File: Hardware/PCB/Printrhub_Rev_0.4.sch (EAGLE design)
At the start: 72 parts, among them J1 DM3D-SF, SW1 SPST_TACT-KMR2, SW2 SPST_TACT-KMR2, U1 MK20DX256VLH7, U2 AP1117E, U3 MAX308-SOT23, Y2 16Mhz/8pF

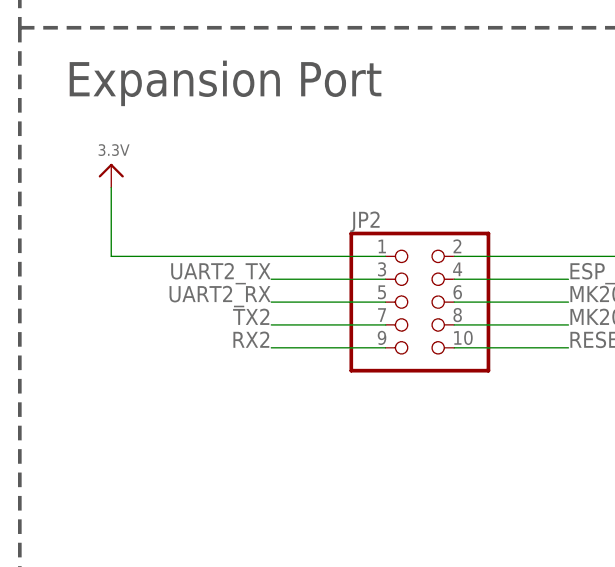
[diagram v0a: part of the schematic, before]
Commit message: Readded SCL1 and SDA1 (so this version is committed, too).
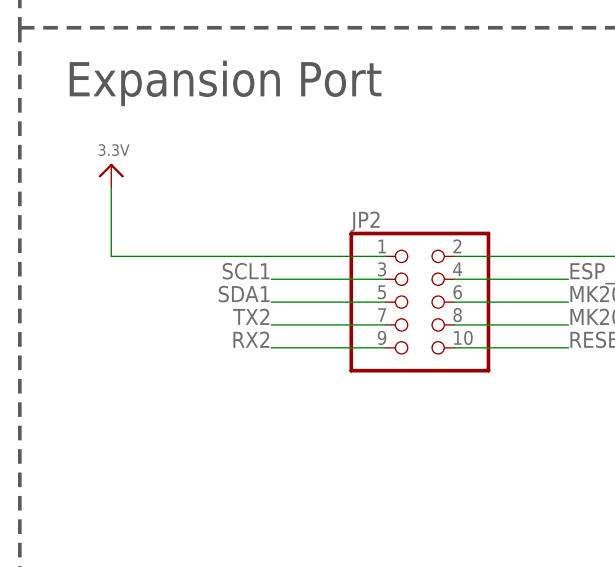
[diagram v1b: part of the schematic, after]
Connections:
- net SCL1: now also JP2.3
- net SDA1: now also JP2.5
- net UART2_RX: no longer JP2.5
- net UART2_TX: no longer JP2.3
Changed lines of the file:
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@@
 <label x="162.56" y="30.48" size="1.778" layer="95" rot="MR0"/>
-</segment>
-<segment>
-<pinref part="JP2" gate="A" pin="5"/>
-<wire x1="-71.12" y1="-104.14" x2="-83.82" y2="-104.14" width="0.1524" layer="91"/>
-<label x="-83.82" y="-104.14" size="1.778" layer="95" rot="MR0"/>
 </segment>
 </net>
@@
 <wire x1="177.8" y1="38.1" x2="162.56" y2="38.1" width="0.1524" layer="91"/>
 <label x="162.56" y="38.1" size="1.778" layer="95" rot="MR0"/>
-</segment>
-<segment>
-<pinref part="JP2" gate="A" pin="3"/>
-<wire x1="-71.12" y1="-101.6" x2="-83.82" y2="-101.6" width="0.1524" layer="91"/>
-<label x="-83.82" y="-101.6" size="1.778" layer="95" rot="MR0"/>
 </segment>
 </net>
@@
 <label x="187.96" y="-149.86" size="1.778" layer="95"/>
 </segment>
+<segment>
+<pinref part="JP2" gate="A" pin="3"/>
+<wire x1="-71.12" y1="-101.6" x2="-83.82" y2="-101.6" width="0.1524" layer="91"/>
+<label x="-83.82" y="-101.6" size="1.778" layer="95" rot="MR0"/>
+</segment>
 </net>
 <net name="SDA1" class="0">
@@
 <label x="187.96" y="-147.32" size="1.778" layer="95"/>
 </segment>
-</net>
+<segment>
+<pinref part="JP2" gate="A" pin="5"/>
+<wire x1="-71.12" y1="-104.14" x2="-83.82" y2="-104.14" width="0.1524" layer="91"/>
+<label x="-83.82" y="-104.14" size="1.778" layer="95" rot="MR0"/>
+</segment>
+</net>

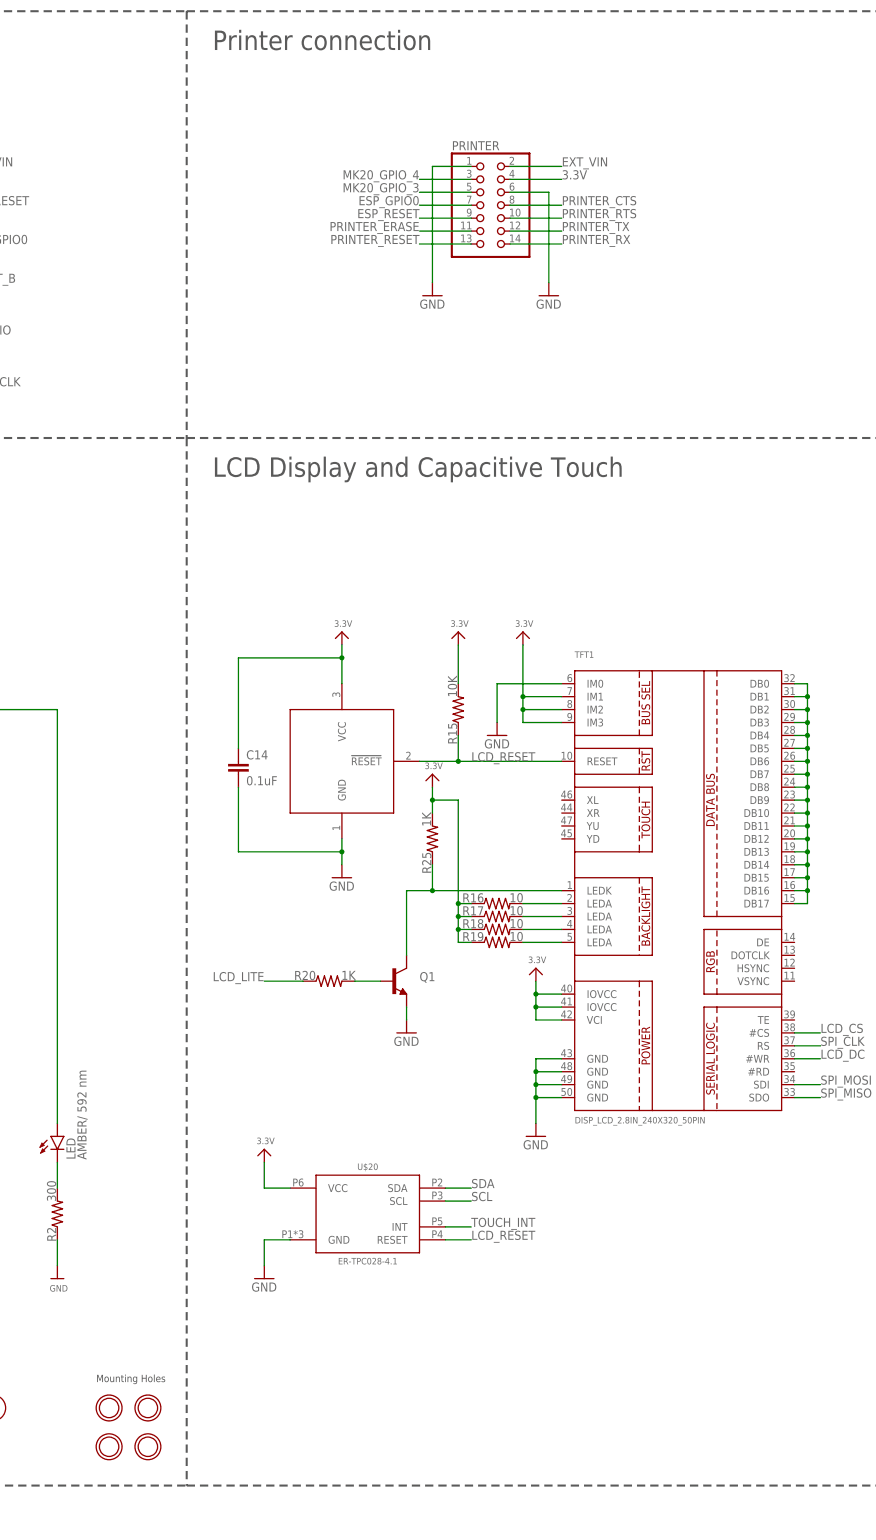
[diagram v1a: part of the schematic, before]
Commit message: Added pull-up and pull-down resistors for PRINTER_RESET and PRINTER_ERASE signals. Replaced plated mounting holes with larger holes (without plate). Moved a few parts for nicer layout.
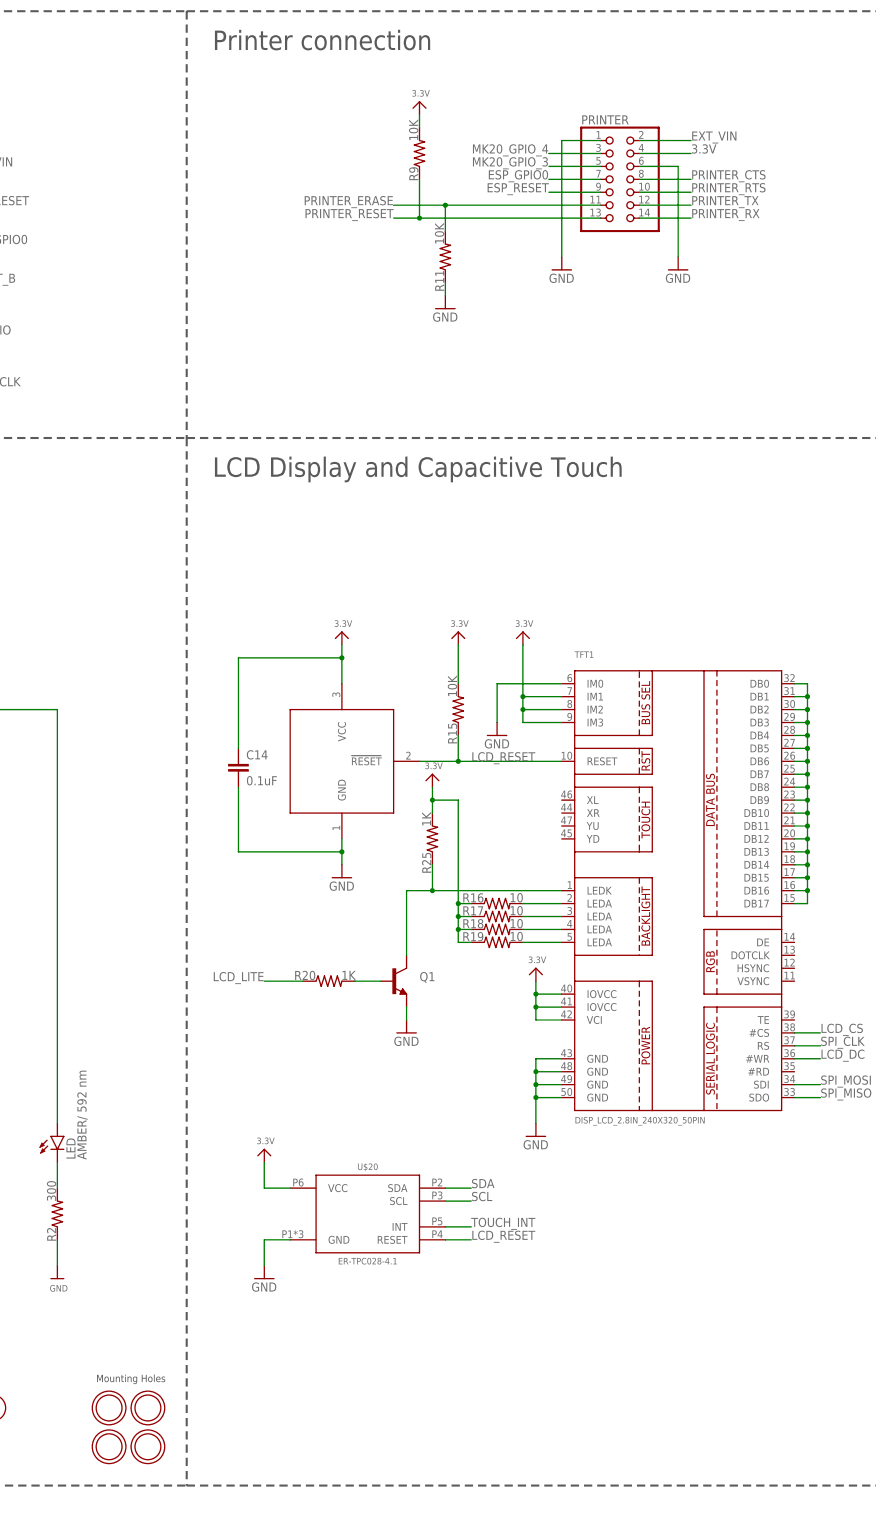
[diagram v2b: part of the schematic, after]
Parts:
- added R11, R9: 10K, appfruits:RESISTOR-10K
- U$15, U$16, U$17, U$18: value MOUNTINGHOLE2.0 -> MOUNTINGHOLE; device microbuilder:MOUNTINGHOLE2.0 -> appfruits:MOUNTINGHOLE
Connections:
- net 3.3V: now also R9.2
- net GND: now also R11.1
- net PRINTER_ERASE: now also R11.2
- net PRINTER_RESET: now also R9.1
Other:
- moved on the sheet: PRINTER
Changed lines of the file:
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@@
 <part name="R6" library="appfruits" deviceset="RESISTOR" device="-1K" value="1K"/>
 <part name="TFT1" library="appfruits" deviceset="DISP_LCD_2.8IN_240X320_50PIN" device=""/>
-<part name="U$15" library="microbuilder" deviceset="MOUNTINGHOLE" device="2.0"/>
-<part name="U$16" library="microbuilder" deviceset="MOUNTINGHOLE" device="2.0"/>
-<part name="U$17" library="microbuilder" deviceset="MOUNTINGHOLE" device="2.0"/>
-<part name="U$18" library="microbuilder" deviceset="MOUNTINGHOLE" device="2.0"/>
+<part name="U$15" library="appfruits" deviceset="MOUNTINGHOLE" device="" value="MOUNTINGHOLE"/>
+<part name="U$16" library="appfruits" deviceset="MOUNTINGHOLE" device="" value="MOUNTINGHOLE"/>
+<part name="U$17" library="appfruits" deviceset="MOUNTINGHOLE" device="" value="MOUNTINGHOLE"/>
+<part name="U$18" library="appfruits" deviceset="MOUNTINGHOLE" device="" value="MOUNTINGHOLE"/>
 <part name="U$21" library="microbuilder" deviceset="3.3V" device=""/>
 <part name="R13" library="appfruits" deviceset="RESISTOR" device="-10K" value="10K"/>
@@
 <part name="SWD_IO" library="appfruits" deviceset="TPV" device="-SMD-18RN"/>
 <part name="SWD_CLK" library="appfruits" deviceset="TPV" device="-SMD-18RN"/>
+<part name="R9" library="appfruits" deviceset="RESISTOR" device="-10K" value="10K"/>
+<part name="U$35" library="microbuilder" deviceset="3.3V" device=""/>
+<part name="R11" library="appfruits" deviceset="RESISTOR" device="-10K" value="10K"/>
+<part name="GND10" library="supply1" deviceset="GND" device=""/>
 </parts>
 <sheets>
@@
 <instance part="R25" gate="G$1" x="294.64" y="-93.98" rot="R90"/>
 <instance part="U$4" gate="G$1" x="294.64" y="-81.28"/>
-<instance part="PRINTER" gate="A" x="304.8" y="30.48"/>
+<instance part="PRINTER" gate="A" x="330.2" y="35.56"/>
 <instance part="FTDI" gate="G$1" x="-38.1" y="-43.18"/>
 <instance part="GND18" gate="1" x="-27.94" y="-53.34"/>
 <instance part="JP3" gate="G$1" x="-101.6" y="0"/>
 <instance part="GND19" gate="1" x="-76.2" y="-10.16"/>
-<instance part="GND16" gate="1" x="294.64" y="12.7"/>
-<instance part="GND17" gate="1" x="317.5" y="12.7"/>
+<instance part="GND16" gate="1" x="320.04" y="17.78"/>
+<instance part="GND17" gate="1" x="342.9" y="17.78"/>
 <instance part="GND20" gate="1" x="15.24" y="-10.16"/>
 <instance part="GND21" gate="1" x="106.68" y="-10.16"/>
@@
 <instance part="SWD_IO" gate="G$1" x="187.96" y="7.62"/>
 <instance part="SWD_CLK" gate="G$1" x="187.96" y="-2.54"/>
+<instance part="R9" gate="G$1" x="292.1" y="40.64" rot="R90"/>
+<instance part="U$35" gate="G$1" x="292.1" y="50.8"/>
+<instance part="R11" gate="G$1" x="297.18" y="20.32" rot="R90"/>
+<instance part="GND10" gate="1" x="297.18" y="10.16"/>
 </instances>
 <busses>
@@
 <segment>
 <pinref part="PRINTER" gate="A" pin="1"/>
-<wire x1="302.26" y1="38.1" x2="294.64" y2="38.1" width="0.1524" layer="91"/>
+<wire x1="327.66" y1="43.18" x2="320.04" y2="43.18" width="0.1524" layer="91"/>
 <pinref part="GND16" gate="1" pin="GND"/>
-<wire x1="294.64" y1="38.1" x2="294.64" y2="15.24" width="0.1524" layer="91"/>
+<wire x1="320.04" y1="43.18" x2="320.04" y2="20.32" width="0.1524" layer="91"/>
 </segment>
 <segment>
 <pinref part="PRINTER" gate="A" pin="6"/>
-<wire x1="309.88" y1="33.02" x2="317.5" y2="33.02" width="0.1524" layer="91"/>
+<wire x1="335.28" y1="38.1" x2="342.9" y2="38.1" width="0.1524" layer="91"/>
 <pinref part="GND17" gate="1" pin="GND"/>
-<wire x1="317.5" y1="33.02" x2="317.5" y2="15.24" width="0.1524" layer="91"/>
+<wire x1="342.9" y1="38.1" x2="342.9" y2="20.32" width="0.1524" layer="91"/>
 </segment>
 <segment>
@@
 <wire x1="-30.48" y1="-99.06" x2="-30.48" y2="-111.76" width="0.1524" layer="91"/>
 <pinref part="GND5" gate="1" pin="GND"/>
+</segment>
+<segment>
+<pinref part="R11" gate="G$1" pin="1"/>
+<pinref part="GND10" gate="1" pin="GND"/>
+<wire x1="297.18" y1="15.24" x2="297.18" y2="12.7" width="0.1524" layer="91"/>
 </segment>
 </net>
@@
 <segment>
 <pinref part="PRINTER" gate="A" pin="4"/>
-<wire x1="309.88" y1="35.56" x2="320.04" y2="35.56" width="0.1524" layer="91"/>
-<label x="320.04" y="35.56" size="1.778" layer="95"/>
+<wire x1="335.28" y1="40.64" x2="345.44" y2="40.64" width="0.1524" layer="91"/>
+<label x="345.44" y="40.64" size="1.778" layer="95"/>
 </segment>
 <segment>
@@
 <wire x1="-71.12" y1="-99.06" x2="-101.6" y2="-99.06" width="0.1524" layer="91"/>
 <wire x1="-101.6" y1="-99.06" x2="-101.6" y2="-91.44" width="0.1524" layer="91"/>
+</segment>
+<segment>
+<pinref part="U$35" gate="G$1" pin="3.3V"/>
+<pinref part="R9" gate="G$1" pin="2"/>
+<wire x1="292.1" y1="48.26" x2="292.1" y2="45.72" width="0.1524" layer="91"/>
 </segment>
 </net>
@@
 <segment>
 <pinref part="PRINTER" gate="A" pin="7"/>
-<wire x1="302.26" y1="30.48" x2="292.1" y2="30.48" width="0.1524" layer="91"/>
-<label x="292.1" y="30.48" size="1.778" layer="99" rot="MR0"/>
+<wire x1="327.66" y1="35.56" x2="317.5" y2="35.56" width="0.1524" layer="91"/>
+<label x="317.5" y="35.56" size="1.778" layer="99" rot="MR0"/>
 </segment>
 <segment>
@@
 <segment>
 <pinref part="PRINTER" gate="A" pin="9"/>
-<wire x1="302.26" y1="27.94" x2="292.1" y2="27.94" width="0.1524" layer="91"/>
-<label x="292.1" y="27.94" size="1.778" layer="99" rot="MR0"/>
+<wire x1="327.66" y1="33.02" x2="317.5" y2="33.02" width="0.1524" layer="91"/>
+<label x="317.5" y="33.02" size="1.778" layer="99" rot="MR0"/>
 </segment>
 <segment>
@@
 <segment>
 <pinref part="PRINTER" gate="A" pin="12"/>
-<wire x1="309.88" y1="25.4" x2="320.04" y2="25.4" width="0.1524" layer="91"/>
-<label x="320.04" y="25.4" size="1.778" layer="95"/>
+<wire x1="335.28" y1="30.48" x2="345.44" y2="30.48" width="0.1524" layer="91"/>
+<label x="345.44" y="30.48" size="1.778" layer="95"/>
 </segment>
 </net>
@@
 <segment>
 <pinref part="PRINTER" gate="A" pin="14"/>
-<wire x1="309.88" y1="22.86" x2="320.04" y2="22.86" width="0.1524" layer="91"/>
-<label x="320.04" y="22.86" size="1.778" layer="95"/>
+<wire x1="335.28" y1="27.94" x2="345.44" y2="27.94" width="0.1524" layer="91"/>
+<label x="345.44" y="27.94" size="1.778" layer="95"/>
 </segment>
 </net>
@@
 <segment>
 <pinref part="PRINTER" gate="A" pin="10"/>
-<wire x1="309.88" y1="27.94" x2="320.04" y2="27.94" width="0.1524" layer="91"/>
-<label x="320.04" y="27.94" size="1.778" layer="95"/>
+<wire x1="335.28" y1="33.02" x2="345.44" y2="33.02" width="0.1524" layer="91"/>
+<label x="345.44" y="33.02" size="1.778" layer="95"/>
 </segment>
 <segment>
@@
 <segment>
 <pinref part="PRINTER" gate="A" pin="8"/>
-<wire x1="309.88" y1="30.48" x2="320.04" y2="30.48" width="0.1524" layer="91"/>
-<label x="320.04" y="30.48" size="1.778" layer="95"/>
+<wire x1="335.28" y1="35.56" x2="345.44" y2="35.56" width="0.1524" layer="91"/>
+<label x="345.44" y="35.56" size="1.778" layer="95"/>
 </segment>
 <segment>
@@
 <segment>
 <pinref part="PRINTER" gate="A" pin="11"/>
-<wire x1="302.26" y1="25.4" x2="292.1" y2="25.4" width="0.1524" layer="91"/>
-<label x="292.1" y="25.4" size="1.778" layer="95" rot="MR0"/>
+<wire x1="327.66" y1="30.48" x2="297.18" y2="30.48" width="0.1524" layer="91"/>
+<label x="287.02" y="30.48" size="1.778" layer="95" rot="MR0"/>
+<junction x="297.18" y="30.48"/>
+<wire x1="297.18" y1="30.48" x2="287.02" y2="30.48" width="0.1524" layer="91"/>
+<wire x1="297.18" y1="30.48" x2="297.18" y2="25.4" width="0.1524" layer="91"/>
+<pinref part="R11" gate="G$1" pin="2"/>
 </segment>
 </net>
@@
 <segment>
 <pinref part="PRINTER" gate="A" pin="13"/>
-<wire x1="302.26" y1="22.86" x2="292.1" y2="22.86" width="0.1524" layer="91"/>
-<label x="292.1" y="22.86" size="1.778" layer="95" rot="MR0"/>
+<wire x1="327.66" y1="27.94" x2="292.1" y2="27.94" width="0.1524" layer="91"/>
+<label x="287.02" y="27.94" size="1.778" layer="95" rot="MR0"/>
+<pinref part="R9" gate="G$1" pin="1"/>
+<wire x1="292.1" y1="27.94" x2="287.02" y2="27.94" width="0.1524" layer="91"/>
+<wire x1="292.1" y1="35.56" x2="292.1" y2="27.94" width="0.1524" layer="91"/>
+<junction x="292.1" y="27.94"/>
 </segment>
 </net>
@@
 <segment>
 <pinref part="PRINTER" gate="A" pin="3"/>
-<wire x1="302.26" y1="35.56" x2="292.1" y2="35.56" width="0.1524" layer="91"/>
-<label x="292.1" y="35.56" size="1.778" layer="99" rot="MR0"/>
+<wire x1="327.66" y1="40.64" x2="317.5" y2="40.64" width="0.1524" layer="91"/>
+<label x="317.5" y="40.64" size="1.778" layer="99" rot="MR0"/>
 </segment>
 </net>
@@
 <segment>
 <pinref part="PRINTER" gate="A" pin="5"/>
-<wire x1="302.26" y1="33.02" x2="292.1" y2="33.02" width="0.1524" layer="91"/>
-<label x="292.1" y="33.02" size="1.778" layer="99" rot="MR0"/>
+<wire x1="327.66" y1="38.1" x2="317.5" y2="38.1" width="0.1524" layer="91"/>
+<label x="317.5" y="38.1" size="1.778" layer="99" rot="MR0"/>
 </segment>
 </net>
@@
 <segment>
 <pinref part="PRINTER" gate="A" pin="2"/>
-<wire x1="309.88" y1="38.1" x2="320.04" y2="38.1" width="0.1524" layer="91"/>
-<label x="320.04" y="38.1" size="1.778" layer="95"/>
-</segment>
-<segment>
+<wire x1="335.28" y1="43.18" x2="345.44" y2="43.18" width="0.1524" layer="91"/>
+<label x="345.44" y="43.18" size="1.778" layer="95"/>
+</segment>
+<segment>
